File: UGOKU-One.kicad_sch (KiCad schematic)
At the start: 80 parts, among them J1 ENC/IO, J10 Conn_01x02, J12 Conn_01x02, J2 SERVO, J3 Conn_02x03_Odd_Even, J4 14110213001000, J5 Conn_01x05, J6 Conn_01x02, J7 ENC/IO, J8 DAC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

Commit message: April-22 order spec
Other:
- moved on the sheet: C12, C13, C14, C15, C16, C17, C18, C19, C4, C7, C8, D8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

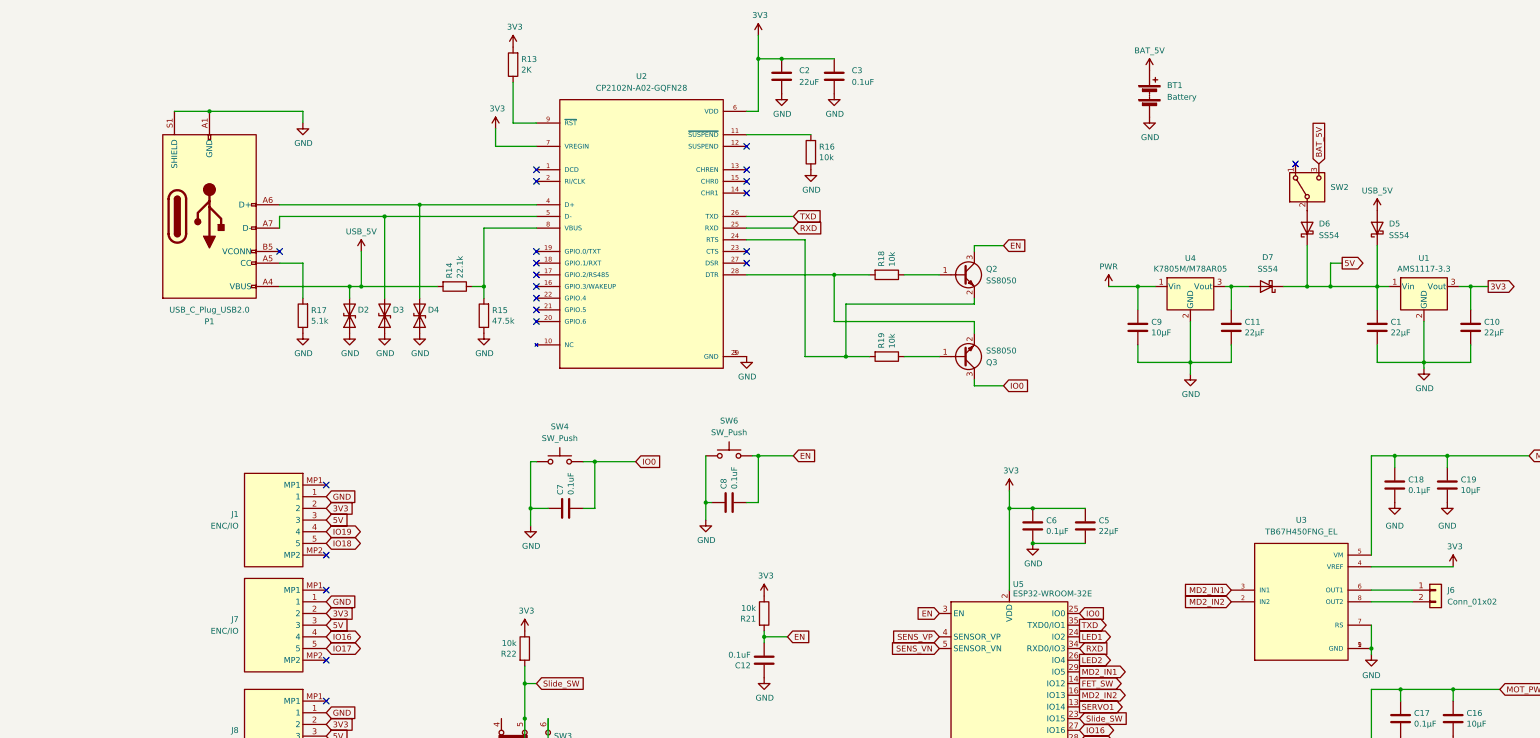
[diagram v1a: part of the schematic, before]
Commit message: correct TXRX, regulator pin assign add batt thermal pad
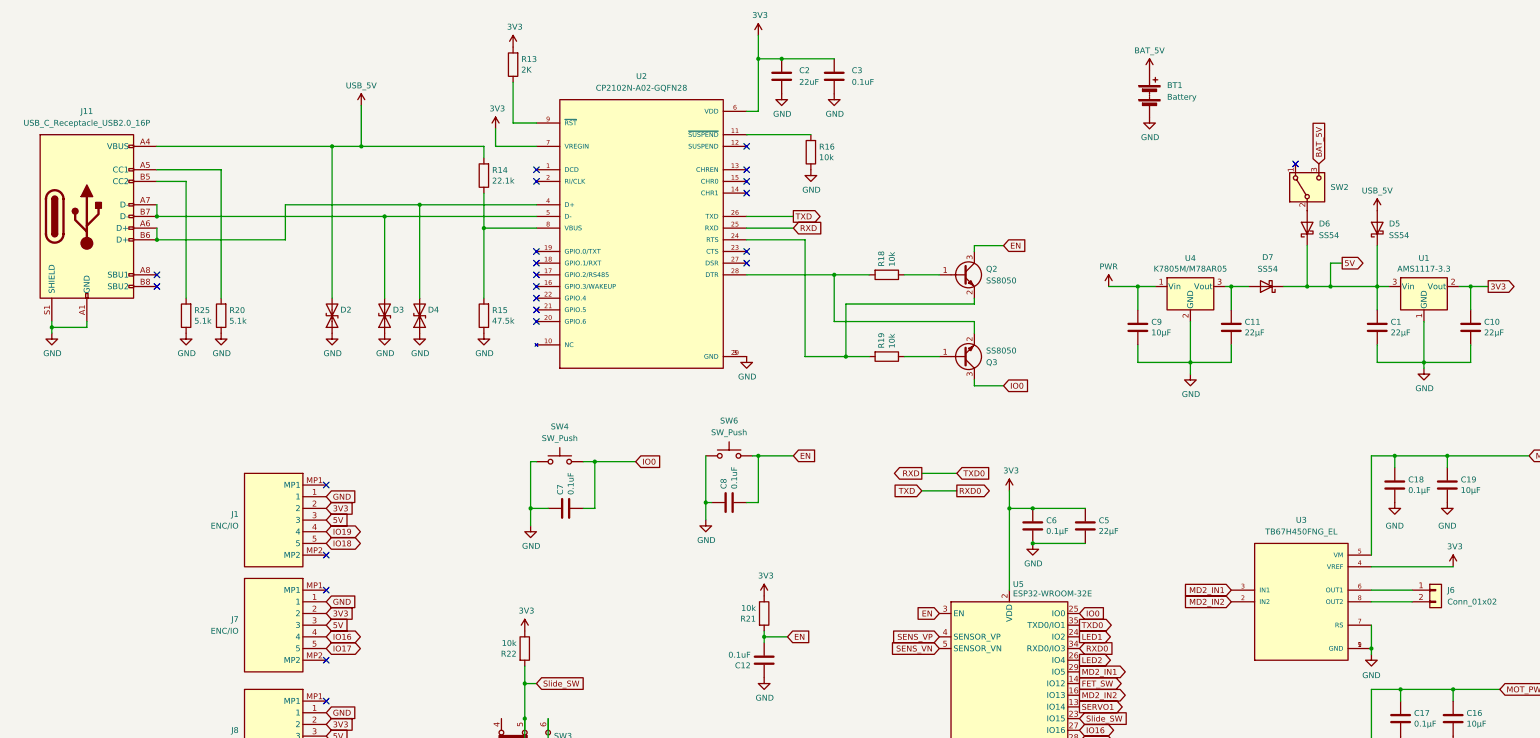
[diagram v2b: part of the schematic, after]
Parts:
- removed P1: USB_C_Plug_USB2.0, Connector_USB:USB_C_Receptacle_GCT_USB4105-xx-A_16P_TopMnt_Horizontal, symbol Connector:USB_C_Plug_USB2.0
- removed R17: 5.1k, Resistor_SMD:R_0402_1005Metric, symbol Device:R
- added J11: USB_C_Receptacle_USB2.0_16P, Connector_USB:USB_C_Receptacle_GCT_USB4105-xx-A_16P_TopMnt_Horizontal, symbol Connector:USB_C_Receptacle_USB2.0_16P
- added R20, R25: 5.1k, Resistor_SMD:R_0402_1005Metric, symbol Device:R
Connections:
- net 3V3: now also U1.2 (Vout); no longer U1.3 (Vout)
- net 5V: now also U1.3 (Vin); no longer U1.1 (Vin)
- net GND: now also U1.1 (GND), J11.A1 (GND), J11.A12 (GND), J11.B1 (GND), J11.B12 (GND), J11.S1 (SHIELD), R20.1, R25.1; no longer U1.2 (GND)
- net RXD: now also U5.35 (TXD0/IO1); no longer U5.34 (RXD0/IO3)
- net USB_5V: now also J11.A4 (VBUS), J11.A9 (VBUS), J11.B4 (VBUS), J11.B9 (VBUS)
- net at D3.2 (A2), U2.5 (D-): now also J11.A7 (D-), J11.B7 (D-)
- net at D4.2 (A2), U2.4 (D+): now also J11.A6 (D+), J11.B6 (D+)
- net TXD renamed RXD0
- net RXD0: now also U5.34 (RXD0/IO3); no longer U5.35 (TXD0/IO1)
- new net: J11.A5 (CC1), R20.2
- new net: J11.B5 (CC2), R25.2
- no-connect marks 33 -> 34
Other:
- moved on the sheet: D2, R14

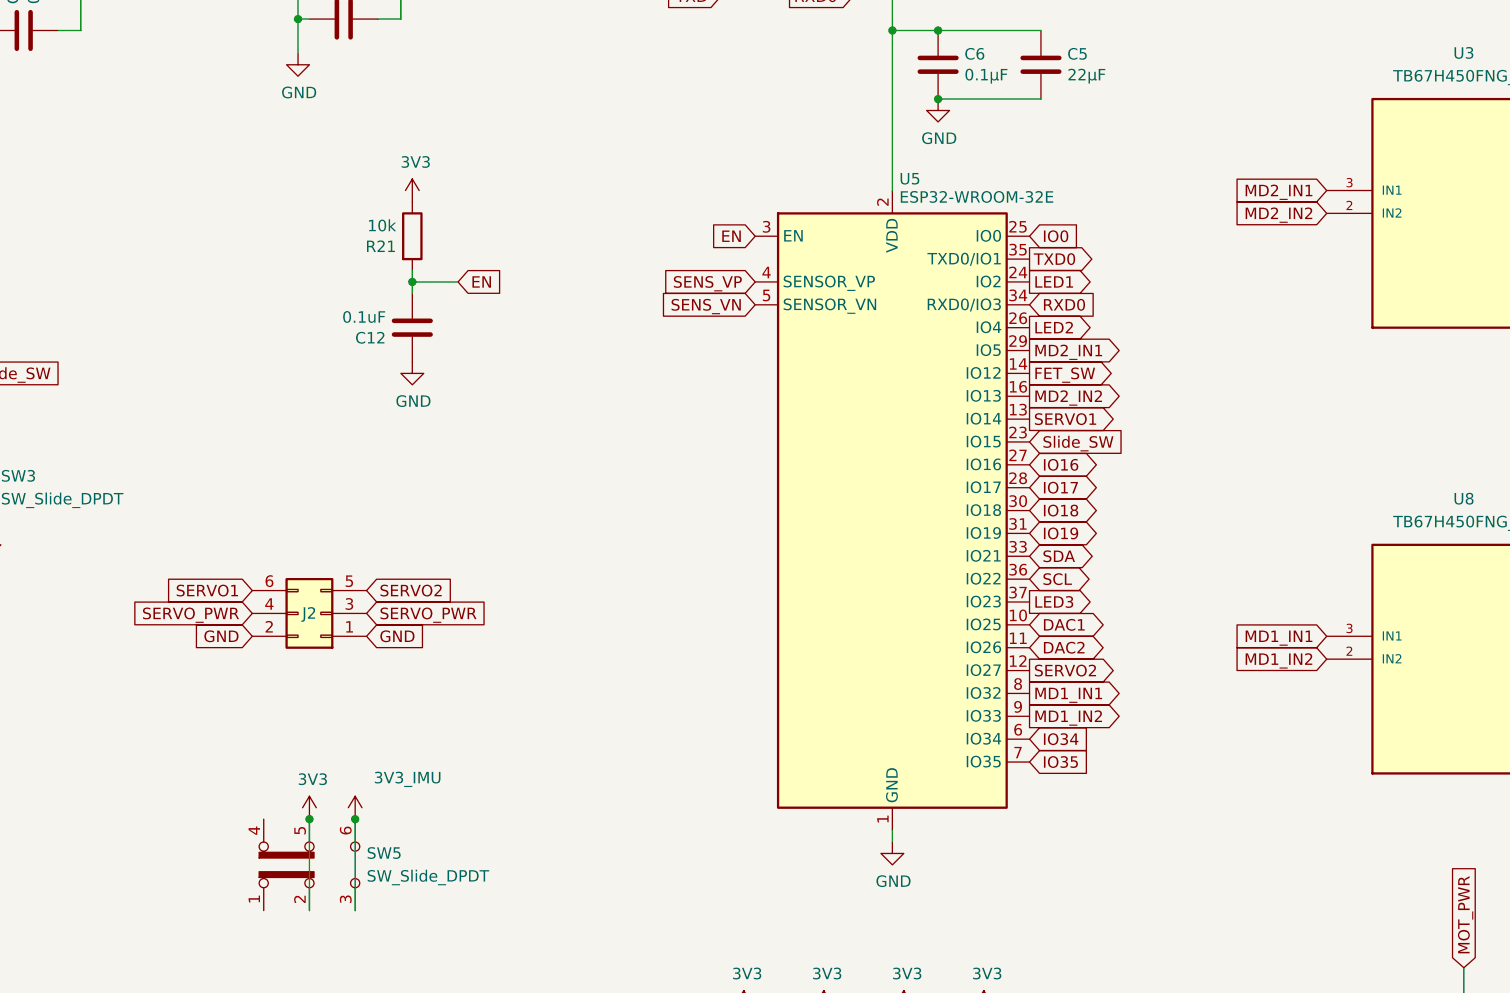
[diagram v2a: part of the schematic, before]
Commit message: add Motor Drive IN1/2 PIN PullDown, IO0 PIN PullUp
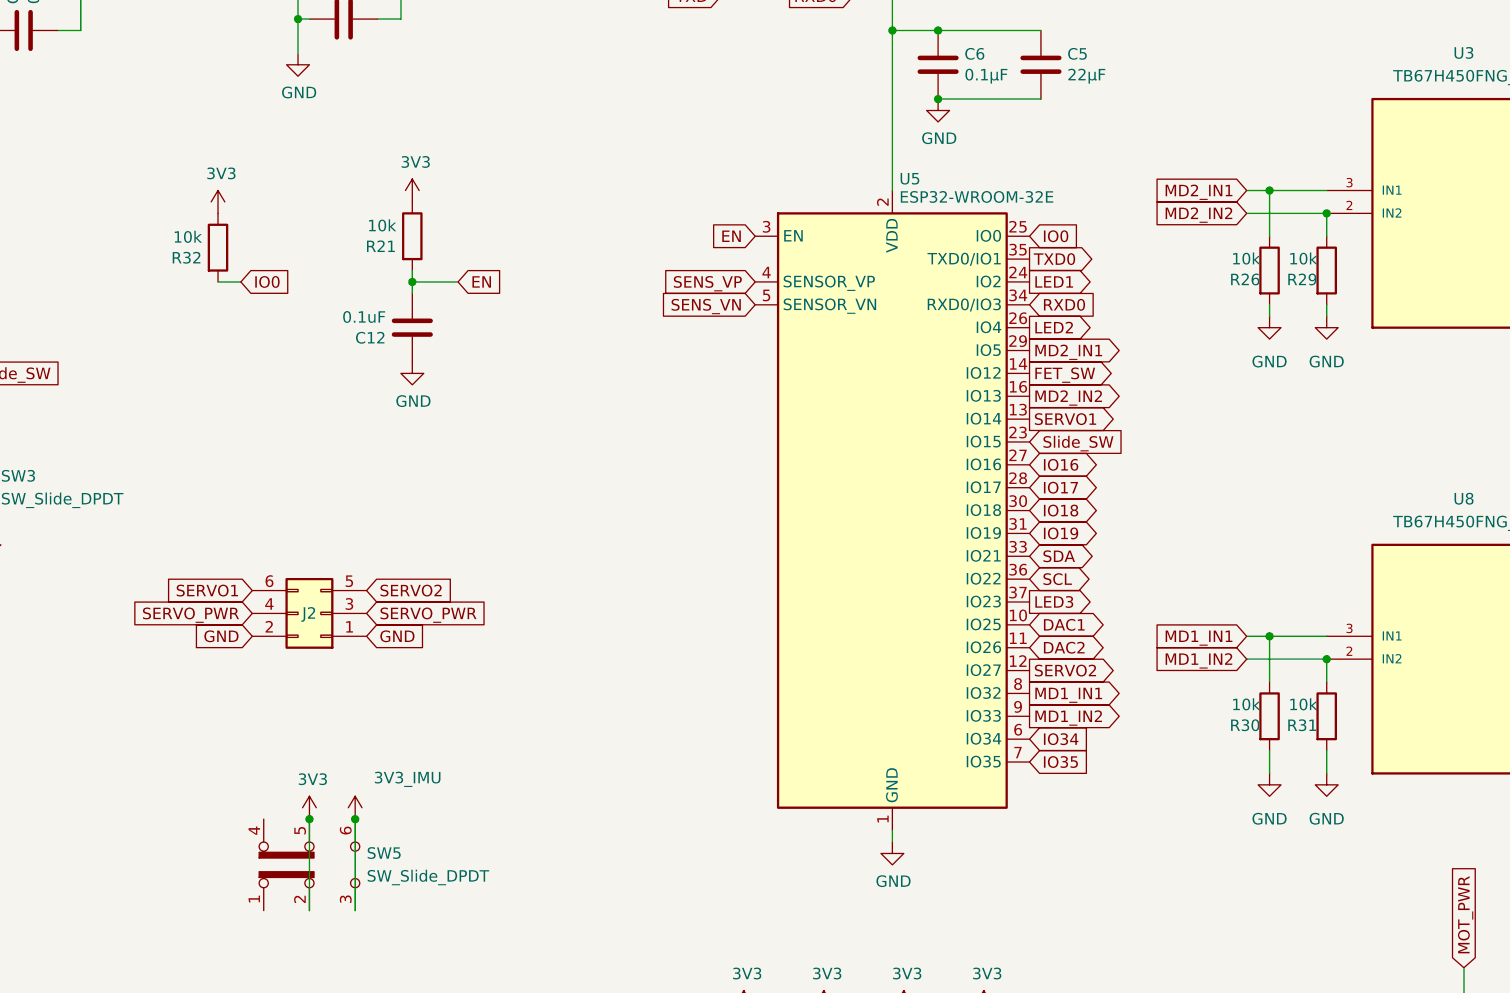
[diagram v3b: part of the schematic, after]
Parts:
- added R26, R29, R30, R31, R32: 10k, Resistor_SMD:R_0402_1005Metric, symbol Device:R
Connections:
- net 3V3: now also R32.1
- net GND: now also R26.2, R29.2, R30.2, R31.2
- net IO0: now also R32.2
- net MD1_IN1: now also R30.1
- net MD1_IN2: now also R31.1
- net MD2_IN1: now also R26.1
- net MD2_IN2: now also R29.1

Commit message: Add Title to sch, Update sch pdf
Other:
- company: (none) -> UGOKU Lab
- title: (none) -> UGOKU One V 1.1.0
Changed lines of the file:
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@@
 	(generator_version "9.0")
 	(paper "A2")
+	(title_block
+		(title "UGOKU One V 1.1.0")
+		(date "2025-06-12")
+		(company "UGOKU Lab")
+	)
 	(junction
 		(at 219.71 327.66)

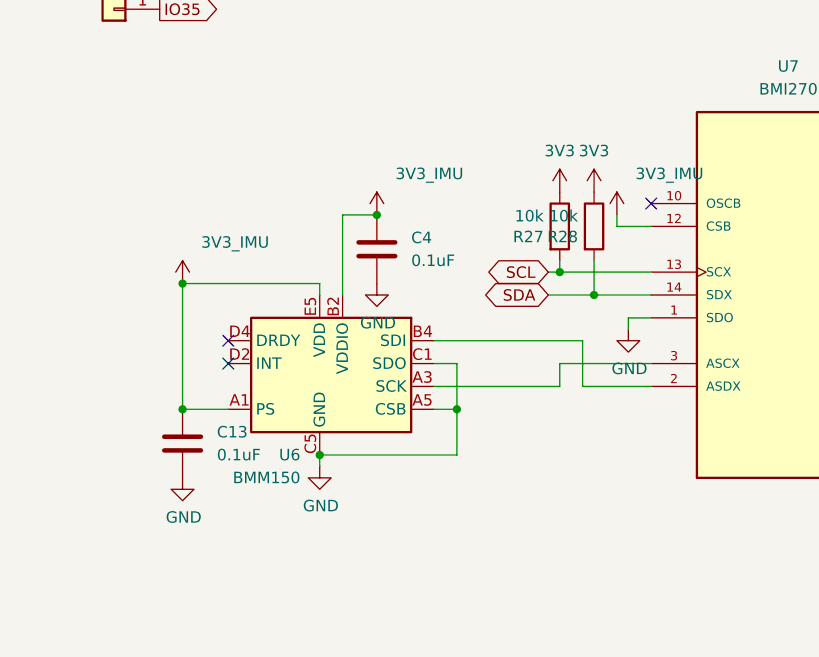
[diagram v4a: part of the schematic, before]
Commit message: JLCPCBの要求に対応するため最小viaサイズを0.3/0.5に変更、JLCPCBの要求に対応するためvia-Padクリアランス確保のため地磁気センサBMM150を廃止、スイッチング出力用FETのピン配置を修正
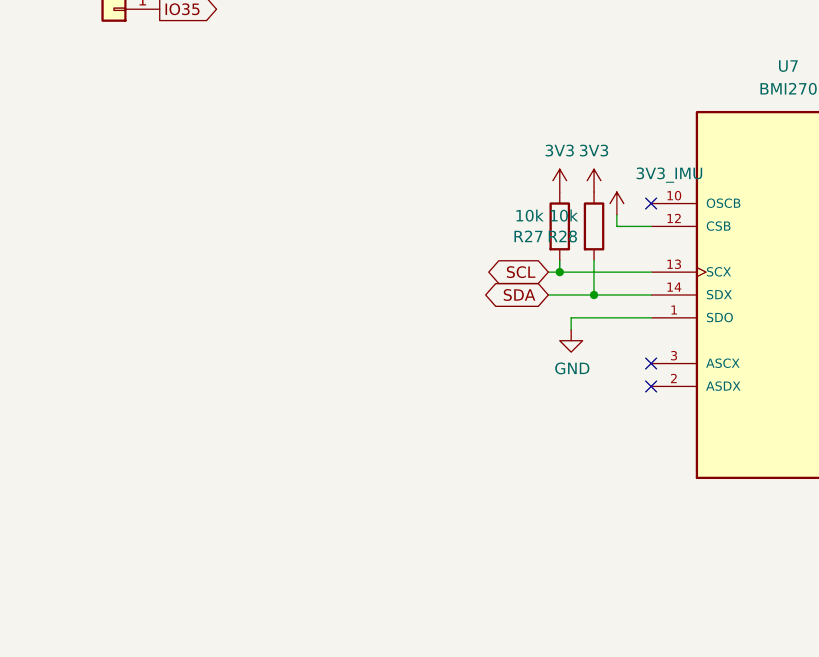
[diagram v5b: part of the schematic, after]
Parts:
- removed C13, C4: 0.1uF, Capacitor_SMD:C_0402_1005Metric, symbol Device:C
- removed U6: BMM150, Package_CSP:WLCSP-12_1.56x1.56mm_P0.4mm, symbol Sensor_Magnetic:BMM150
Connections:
- net GND: now also Q1.2 (S); no longer Q1.3 (S)
- net at D8.2 (A), J4.2: now also Q1.3 (D); no longer Q1.1 (D)
- net at R23.1, R24.1: now also Q1.1 (G); no longer Q1.2 (G)

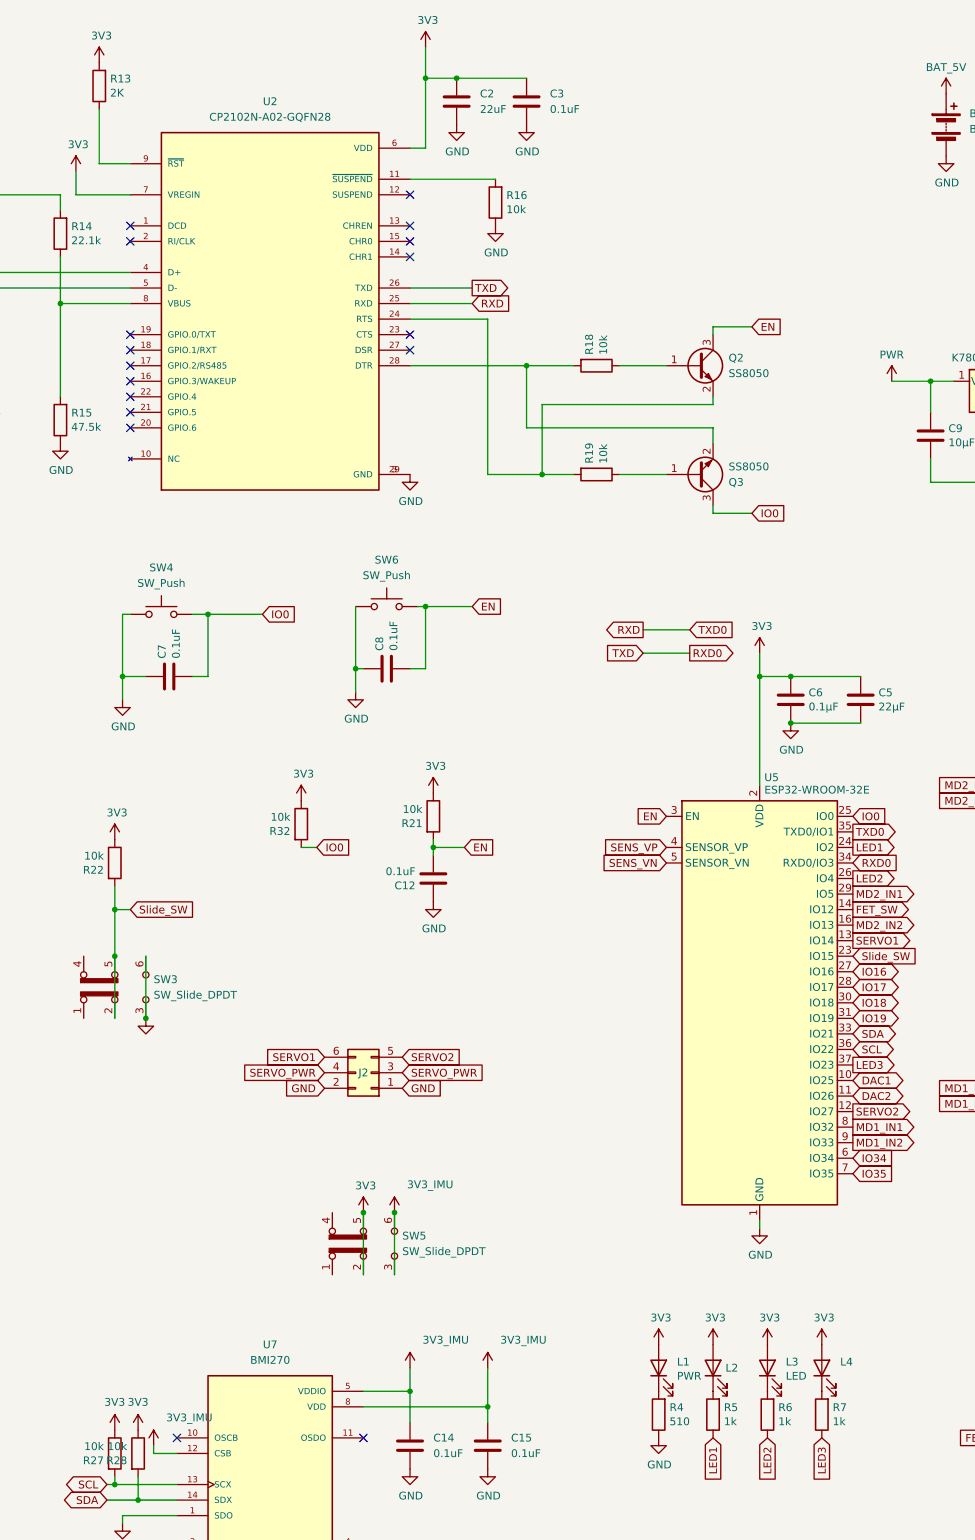
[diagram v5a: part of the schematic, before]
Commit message: IMUの待機電力が微小のため、IMUの電源スイッチを廃止
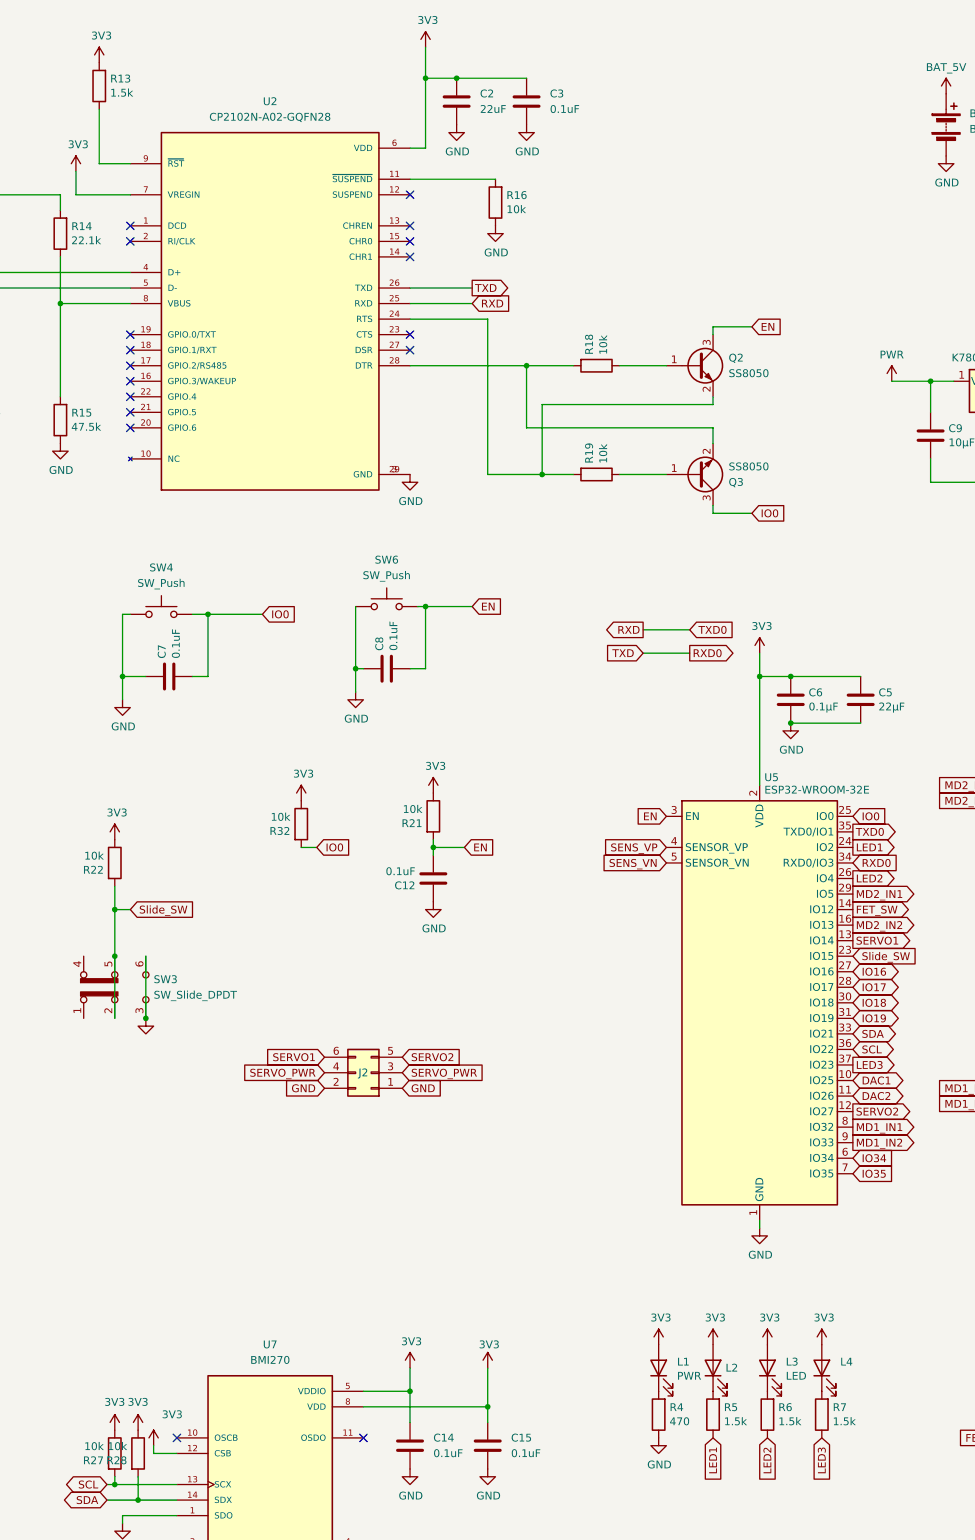
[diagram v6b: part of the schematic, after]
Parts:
- removed SW5: SW_Slide_DPDT, 0_UGOKU-One_Lib:SSSS213202, symbol Switch:SW_Slide_DPDT
- R13: value 2K -> 1.5k
- R4: value 510 -> 470
- R5, R6, R7: value 1k -> 1.5k
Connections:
- net 3V3_IMU is gone; now on net 3V3: C14.1, C15.1, U7.12 (CSB), U7.5 (VDDIO), U7.8 (VDD)
